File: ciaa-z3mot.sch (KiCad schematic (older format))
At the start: 74 parts, among them J1 Conn_01x20, J2 Conn_01x20, J3 Conn_01x02, J4 SWD, J5 USB_OTG, J6 Conn_Coaxial, J7 Conn_01x05, J8 Conn_Coaxial, SW1 reset, SW2 reset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

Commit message: mejoras 1
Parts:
- removed J3: Conn_01x02, Connector_PinHeader_2.54mm:PinHeader_1x02_P2.54mm_Vertical, symbol Connector_Generic:Conn_01x02
- added D4: ON, footprints:LED_0805, symbol ciaa-z3r0:LED_ALT
- added R12: 1K, Resistor_SMD:R_0402_1005Metric, symbol ciaa-z3r0:R_Small
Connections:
- net PA2 is gone; now on net ENA: J2.13 (Pin_13), U1.15 (GPIO2)
- net PA8 is gone; now on net +3V3: J1.17 (Pin_17), R4.2
- net PC1 is gone; now on net GND: J2.15 (Pin_15)
- net SDA is gone; now on net GPIO03: U2.3 (SDA)
- net +3V3: now also R12.2
- net Bat: now also J1.20 (Pin_20)
- net GND: now also D4.1 (K); no longer J1.19 (Pin_19), J1.20 (Pin_20)
- net On: now also J1.19 (Pin_19)
- net B_USB+: no longer names the net of J5.3 (D+), U3.6 (IO1_B), U5.3 (D+)
- net B_USB-: no longer names the net of J5.2 (D-), U3.4 (IO2_B), U5.2 (D-)
- net PA10 renamed GPIO01
- net PA9 renamed GPIO0
- net GPIO0: no longer U1.25 (GPIO0)
- net PC0 renamed GPIO03
- net SCL renamed GPIO00
- net GPIO00: now also U1.25 (GPIO0)
- new net: D4.2 (A), R12.1

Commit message: sin verificar ruteo gnd
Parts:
- removed D4: ON, footprints:LED_0805, symbol ciaa-z3r0:LED_ALT
- removed J5: USB_OTG, footprints:USB_Micro-B_Molex_47346-0001, symbol ciaa-z3r0:USB_OTG
- added J3: Conn_01x02, Connector_PinHeader_1.27mm:PinHeader_1x02_P1.27mm_Vertical, symbol Connector_Generic:Conn_01x02
- added J5: Conn_01x04, Connector_PinHeader_1.27mm:PinHeader_1x04_P1.27mm_Vertical, symbol Connector_Generic:Conn_01x04
- added R13: 0R, Resistor_SMD:R_0201_0603Metric, symbol ciaa-z3r0:R_Small
- R12: value 1K -> 0R; footprint Resistor_SMD:R_0402_1005Metric -> Resistor_SMD:R_0201_0603Metric
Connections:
- net GPIO00 is gone; now on net GPIO0: U1.25 (GPIO0), U2.1 (SCL)
- net PC2 is gone; now on net GND: J2.16 (Pin_16)
- net PC4 is gone; now on net GND: J2.18 (Pin_18)
- net +3V3: no longer J1.17 (Pin_17), R12.2, R4.2
- net Bat: now also J3.2 (Pin_2); no longer J1.20 (Pin_20)
- net GND: now also J1.19 (Pin_19), J1.20 (Pin_20), J5.4 (Pin_4)
- net LFXTAL_N: now also R12.2; no longer J2.20 (Pin_20), R3.2, SW1.2
- net LFXTAL_P: now also R13.2; no longer J2.19 (Pin_19)
- net On: now also J3.1 (Pin_1); no longer J1.19 (Pin_19)
- net vusb: now also J5.1 (Pin_1)
- net at U3.4 (IO2_B), U5.2 (D-): now also J5.2 (Pin_2)
- net at U3.6 (IO1_B), U5.3 (D+): now also J5.3 (Pin_3)
- net PB8: now reaches R12.1
- net PB8: now also J2.20 (Pin_20), R3.2, SW1.2
- new net PA8: J1.17 (Pin_17), R4.2
- new net PB7: J2.19 (Pin_19), R13.1
- no-connect marks 5 -> 3
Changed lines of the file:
@@
 Text Label 4900 2325 0    60   ~ 0
 PD4
-Text Label 4900 3225 0    60   ~ 0
+Text Label 6000 3225 0    60   ~ 0
 PB7
-Text Label 4900 3125 0    60   ~ 0
+Text Label 6000 3125 0    60   ~ 0
 PB8
 Text Label 4900 2925 0    60   ~ 0
@@
 $EndComp
 $Comp
-L ciaa-z3r0:USB_OTG J5
-U 1 1 59D07BDE
-P 9025 3450
-F 0 "J5" H 9081 3917 50  0000 C CNN
-F 1 "USB_OTG" H 9000 3850 50  0000 C CNN
-F 2 "footprints:USB_Micro-B_Molex_47346-0001" H 9175 3400 50  0001 C CNN
-F 3 "" H 9175 3400 50  0001 C CNN
-	1    9025 3450
-	-1   0    0    -1
-$EndComp
-$Comp
 L ciaa-z3r0:R_Small R7
 U 1 1 59D08165
@@
 	1    0    0    -1
 $EndComp
-NoConn ~ 9125 3850
-NoConn ~ 8725 3650
 $Comp
 L ciaa-z3r0:GND #PWR040
@@
 L ciaa-z3r0:GND #PWR052
 U 1 1 59D09A9B
-P 9025 3950
-F 0 "#PWR052" H 9025 3700 50  0001 C CNN
-F 1 "GND" H 9030 3822 50  0000 R CNN
-F 2 "" H 9025 3950 50  0001 C CNN
-F 3 "" H 9025 3950 50  0001 C CNN
-	1    9025 3950
+P 8775 3225
+F 0 "#PWR052" H 8775 2975 50  0001 C CNN
+F 1 "GND" H 8780 3097 50  0000 R CNN
+F 2 "" H 8775 3225 50  0001 C CNN
+F 3 "" H 8775 3225 50  0001 C CNN
+	1    8775 3225
 	1    0    0    -1
 $EndComp
@@
 Wire Wire Line
 	8475 3400 8225 3400
-Wire Wire Line
-	9025 3850 9025 3950
 Wire Wire Line
 	7025 3500 6950 3500
@@
 	1    0    0    -1
 $EndComp
-Text Label 8550 3250 2    60   ~ 0
+Text Label 8975 3600 2    60   ~ 0
 vusb
-Wire Wire Line
-	8725 3250 8550 3250
 $Comp
 L ciaa-z3r0:GND #PWR058
@@
 	4900 2825 5850 2825
 Wire Wire Line
-	4900 3125 5175 3125
-Wire Wire Line
-	4900 3225 5175 3225
-Wire Wire Line
 	4900 2625 5175 2625
 Wire Wire Line
@@
 Wire Wire Line
 	8725 3525 8725 3550
-Connection ~ 8725 3550
 Wire Wire Line
 	8725 3375 8725 3450
-Connection ~ 8725 3450
 $Comp
 L Connector_Generic:Conn_01x05 J7
@@
 GPIO01
 Text Label 4900 3425 0    60   ~ 0
-GPIO00
+GPIO0
 Text GLabel 6850 5750 0    60   Input ~ 0
 XIN
@@
 Wire Wire Line
 	3500 4225 3500 4800
-Text Label 850  3225 0    60   ~ 0
-On
-Text Label 850  3125 0    60   ~ 0
-Bat
 Text Label 3200 4225 3    60   ~ 0
 GPIO02
@@
 	5300 3425 4900 3425
 $Comp
-L ciaa-z3r0:LED_ALT D4
-U 1 1 5DC43F19
-P 4100 7075
-F 0 "D4" H 4250 6975 50  0000 C CNN
-F 1 "ON" H 4100 6975 50  0000 C CNN
-F 2 "footprints:LED_0805" H 4100 7075 50  0001 C CNN
-F 3 "" H 4100 7075 50  0001 C CNN
-	1    4100 7075
-	0    -1   -1   0
-$EndComp
-$Comp
-L ciaa-z3r0:R_Small R12
-U 1 1 5DC43F1F
-P 4100 6800
-F 0 "R12" V 4200 6800 50  0000 C CNN
-F 1 "1K" V 4100 6800 50  0000 C CNN
-F 2 "Resistor_SMD:R_0402_1005Metric" H 4100 6800 50  0001 C CNN
-F 3 "" H 4100 6800 50  0001 C CNN
-	1    4100 6800
-	1    0    0    1
-$EndComp
-$Comp
-L ciaa-z3r0:GND #PWR0103
-U 1 1 5DC43F25
-P 4100 7250
-F 0 "#PWR0103" H 4100 7000 50  0001 C CNN
-F 1 "GND" V 4105 7122 50  0000 R CNN
-F 2 "" H 4100 7250 50  0001 C CNN
-F 3 "" H 4100 7250 50  0001 C CNN
-	1    4100 7250
-	1    0    0    -1
-$EndComp
-Text Label 4100 6700 1    60   ~ 0
-PA8
-Wire Wire Line
-	4100 6925 4100 6900
-Wire Wire Line
-	4100 7225 4100 7250
-$Comp
-L ciaa-z3r0:+3.3V #PWR0104
-U 1 1 5DC53C65
-P 4100 6700
-F 0 "#PWR0104" H 4100 6550 50  0001 C CNN
-F 1 "+3.3V" H 4125 6850 50  0000 C CNN
-F 2 "" H 4100 6700 50  0000 C CNN
-F 3 "" H 4100 6700 50  0000 C CNN
-	1    4100 6700
-	1    0    0    -1
-$EndComp
-$Comp
 L ciaa-z3r0:GND #PWR056
 U 1 1 5E1EADF5
@@
 $EndComp
 Wire Wire Line
-	9675 3375 8725 3375
-Wire Wire Line
-	9675 3525 8725 3525
+	9675 3375 8900 3375
+Wire Wire Line
+	9675 3525 8900 3525
 $Comp
 L ciaa-z3mot:USB_PCB_PRINT U5
@@
 	1    0    0    -1
 $EndComp
+$Comp
+L Connector_Generic:Conn_01x02 J3
+U 1 1 5D980732
+P 2875 6500
+F 0 "J3" H 2955 6492 50  0000 L CNN
+F 1 "Conn_01x02" H 2955 6401 50  0000 L CNN
+F 2 "Connector_PinHeader_1.27mm:PinHeader_1x02_P1.27mm_Vertical" H 2875 6500 50  0001 C CNN
+F 3 "~" H 2875 6500 50  0001 C CNN
+	1    2875 6500
+	1    0    0    -1
+$EndComp
+Text Label 2675 6600 2    60   ~ 0
+Bat
+Text Label 2675 6500 2    60   ~ 0
+On
+$Comp
+L Connector_Generic:Conn_01x04 J5
+U 1 1 5DAC98CD
+P 9175 3500
+F 0 "J5" H 9093 3075 50  0000 C CNN
+F 1 "Conn_01x04" H 9093 3166 50  0000 C CNN
+F 2 "Connector_PinHeader_1.27mm:PinHeader_1x04_P1.27mm_Vertical" H 9175 3500 50  0001 C CNN
+F 3 "~" H 9175 3500 50  0001 C CNN
+	1    9175 3500
+	1    0    0    1
+$EndComp
+Wire Wire Line
+	8775 3225 8975 3225
+Wire Wire Line
+	8975 3225 8975 3300
+Wire Wire Line
+	8975 3400 8900 3400
+Wire Wire Line
+	8900 3400 8900 3375
+Connection ~ 8900 3375
+Wire Wire Line
+	8900 3375 8725 3375
+Wire Wire Line
+	8975 3500 8900 3500
+Wire Wire Line
+	8900 3500 8900 3525
+Connection ~ 8900 3525
+Wire Wire Line
+	8900 3525 8725 3525
+$Comp
+L ciaa-z3r0:R_Small R12
+U 1 1 5D958121
+P 5900 3125
+F 0 "R12" V 5750 3125 50  0000 C CNN
+F 1 "0R" V 5825 3125 50  0000 C CNN
+F 2 "Resistor_SMD:R_0201_0603Metric" H 5900 3125 50  0001 C CNN
+F 3 "" H 5900 3125 50  0001 C CNN
+	1    5900 3125
+	0    1    1    0
+$EndComp
+$Comp
+L ciaa-z3r0:R_Small R13
+U 1 1 5D962928
+P 5900 3225
+F 0 "R13" V 5750 3225 50  0000 C CNN
+F 1 "0R" V 5825 3225 50  0000 C CNN
+F 2 "Resistor_SMD:R_0201_0603Metric" H 5900 3225 50  0001 C CNN
+F 3 "" H 5900 3225 50  0001 C CNN
+	1    5900 3225
+	0    1    1    0
+$EndComp
+Wire Wire Line
+	4900 3225 5800 3225
+Wire Wire Line
+	4900 3125 5800 3125
+Wire Wire Line
+	850  3125 850  3225
+Connection ~ 850  3125
+Wire Wire Line
+	850  3125 1150 3125
+Wire Wire Line
+	1150 3125 1150 3100
+$Comp
+L ciaa-z3r0:GND #PWR0103
+U 1 1 5DA736F9
+P 1150 3125
+F 0 "#PWR0103" H 1150 2875 50  0001 C CNN
+F 1 "GND" H 1200 3250 50  0000 R CNN
+F 2 "" H 1150 3125 50  0001 C CNN
+F 3 "" H 1150 3125 50  0001 C CNN
+	1    1150 3125
+	1    0    0    -1
+$EndComp
+Connection ~ 1150 3125
+$Comp
+L ciaa-z3r0:GND #PWR?
+U 1 1 5D954E99
+P 775 1050
+F 0 "#PWR?" H 775 800 50  0001 C CNN
+F 1 "GND" V 780 922 50  0000 R CNN
+F 2 "" H 775 1050 50  0001 C CNN
+F 3 "" H 775 1050 50  0001 C CNN
+	1    775  1050
+	1    0    0    -1
+$EndComp
+Wire Wire Line
+	1050 1050 950  1050
+Wire Wire Line
+	950  1050 950  1250
+Wire Wire Line
+	950  1250 1050 1250
+Wire Wire Line
+	775  1050 950  1050
+Connection ~ 950  1050
 $EndSCHEMATC

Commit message: render completo y cambio smd pack
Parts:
- C33: footprint Capacitor_SMD:C_0603_1608Metric -> Capacitor_SMD:C_0805_2012Metric
- C42: footprint footprints:C_0603 -> Capacitor_SMD:C_1206_3216Metric
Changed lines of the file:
@@
 F 0 "C42" H 6008 6929 50  0000 R CNN
 F 1 "4.7u" H 6008 7020 50  0000 R CNN
-F 2 "footprints:C_0603" H 6100 6975 50  0001 C CNN
+F 2 "Capacitor_SMD:C_1206_3216Metric" H 6100 6975 50  0001 C CNN
 F 3 "" H 6100 6975 50  0001 C CNN
 	1    6100 6975
@@
 F 0 "C33" H 9108 4929 50  0000 R CNN
 F 1 "4.7u" H 9108 5020 50  0000 R CNN
-F 2 "Capacitor_SMD:C_0603_1608Metric" H 9200 4975 50  0001 C CNN
+F 2 "Capacitor_SMD:C_0805_2012Metric" H 9200 4975 50  0001 C CNN
 F 3 "" H 9200 4975 50  0001 C CNN
 	1    9200 4975
@@
 Connection ~ 1150 3125
 $Comp
-L ciaa-z3r0:GND #PWR?
+L ciaa-z3r0:GND #PWR0104
 U 1 1 5D954E99
 P 775 1050
-F 0 "#PWR?" H 775 800 50  0001 C CNN
+F 0 "#PWR0104" H 775 800 50  0001 C CNN
 F 1 "GND" V 780 922 50  0000 R CNN
 F 2 "" H 775 1050 50  0001 C CNN

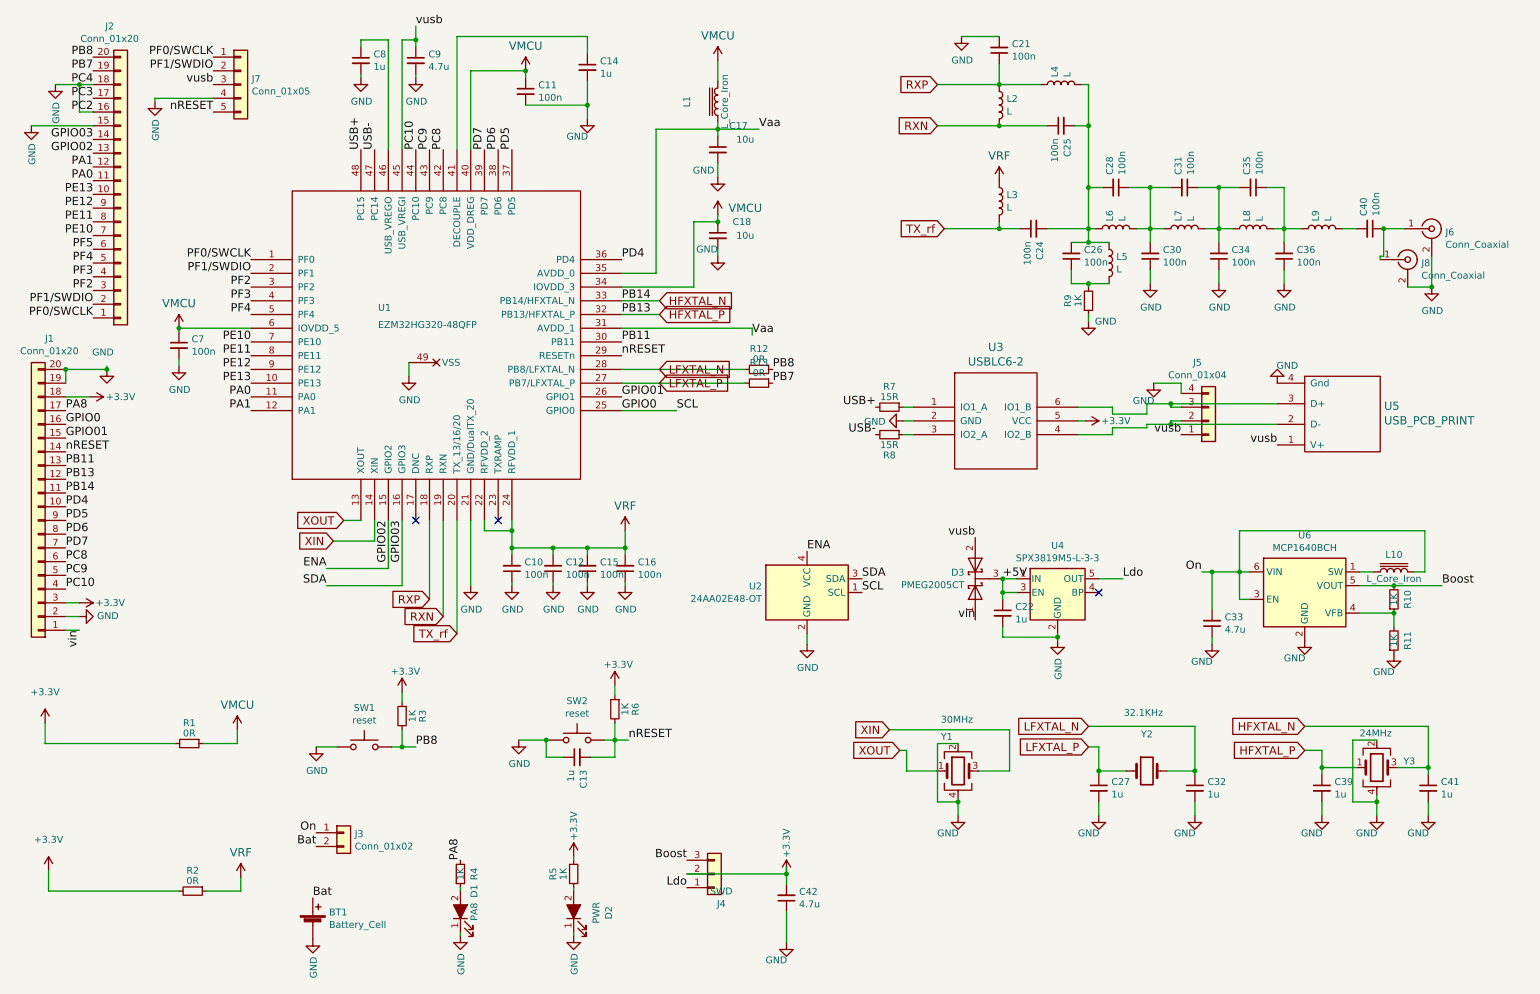
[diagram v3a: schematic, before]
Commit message: BOM
edicion de fb mdp1640 y en el bom
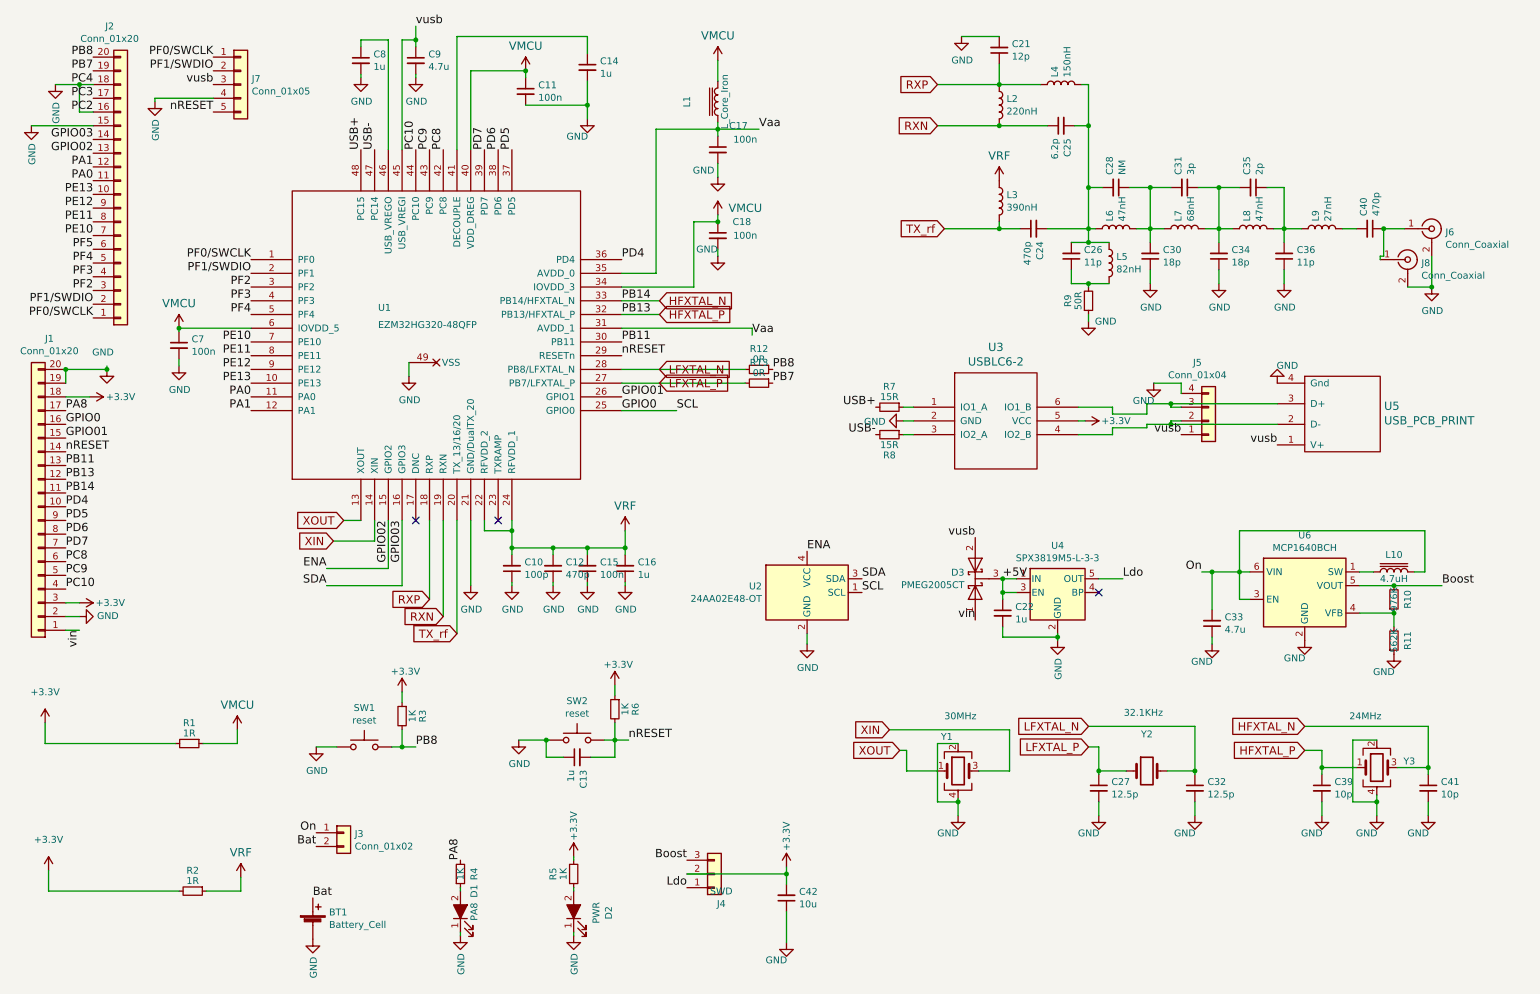
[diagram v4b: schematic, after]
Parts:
- C10: value 100n -> 100p
- C12, C24, C40: value 100n -> 470p
- C13, C22, C8, C9: footprint footprints:C_0603 -> Capacitor_SMD:C_0603_1608Metric
- C16: value 100n -> 1u
- C17, C18: value 10u -> 100n
- C21: value 100n -> 12p
- C25: value 100n -> 6.2p
- C26, C36: value 100n -> 11p
- C27, C32: value 1u -> 12.5p
- C28: value 100n -> NM
- C30, C34: value 100n -> 18p
- C31: value 100n -> 3p
- C35: value 100n -> 2p
- C39, C41: value 1u -> 10p
- C42: value 4.7u -> 10u
- L1: footprint Inductor_SMD:L_0603_1608Metric -> Inductor_SMD:L_0402_1005Metric
- L10: value L_Core_Iron -> 4.7uH; footprint Inductor_SMD:L_Taiyo-Yuden_MD-4040 -> Inductor_SMD:L_1008_2520Metric
- L2: value L -> 220nH
- L3: value L -> 390nH
- L4: value L -> 150nH
- L5: value L -> 82nH
- L6, L8: value L -> 47nH
- L7: value L -> 68nH
- L9: value L -> 27nH
- R1, R2: value 0R -> 1R
- R10: value 1K -> 976K
- R11: value 1K -> 562K
- R9: value 1K -> 50R
